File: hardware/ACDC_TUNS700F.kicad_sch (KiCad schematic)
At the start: 1 part, among them U1 TUNS700F28

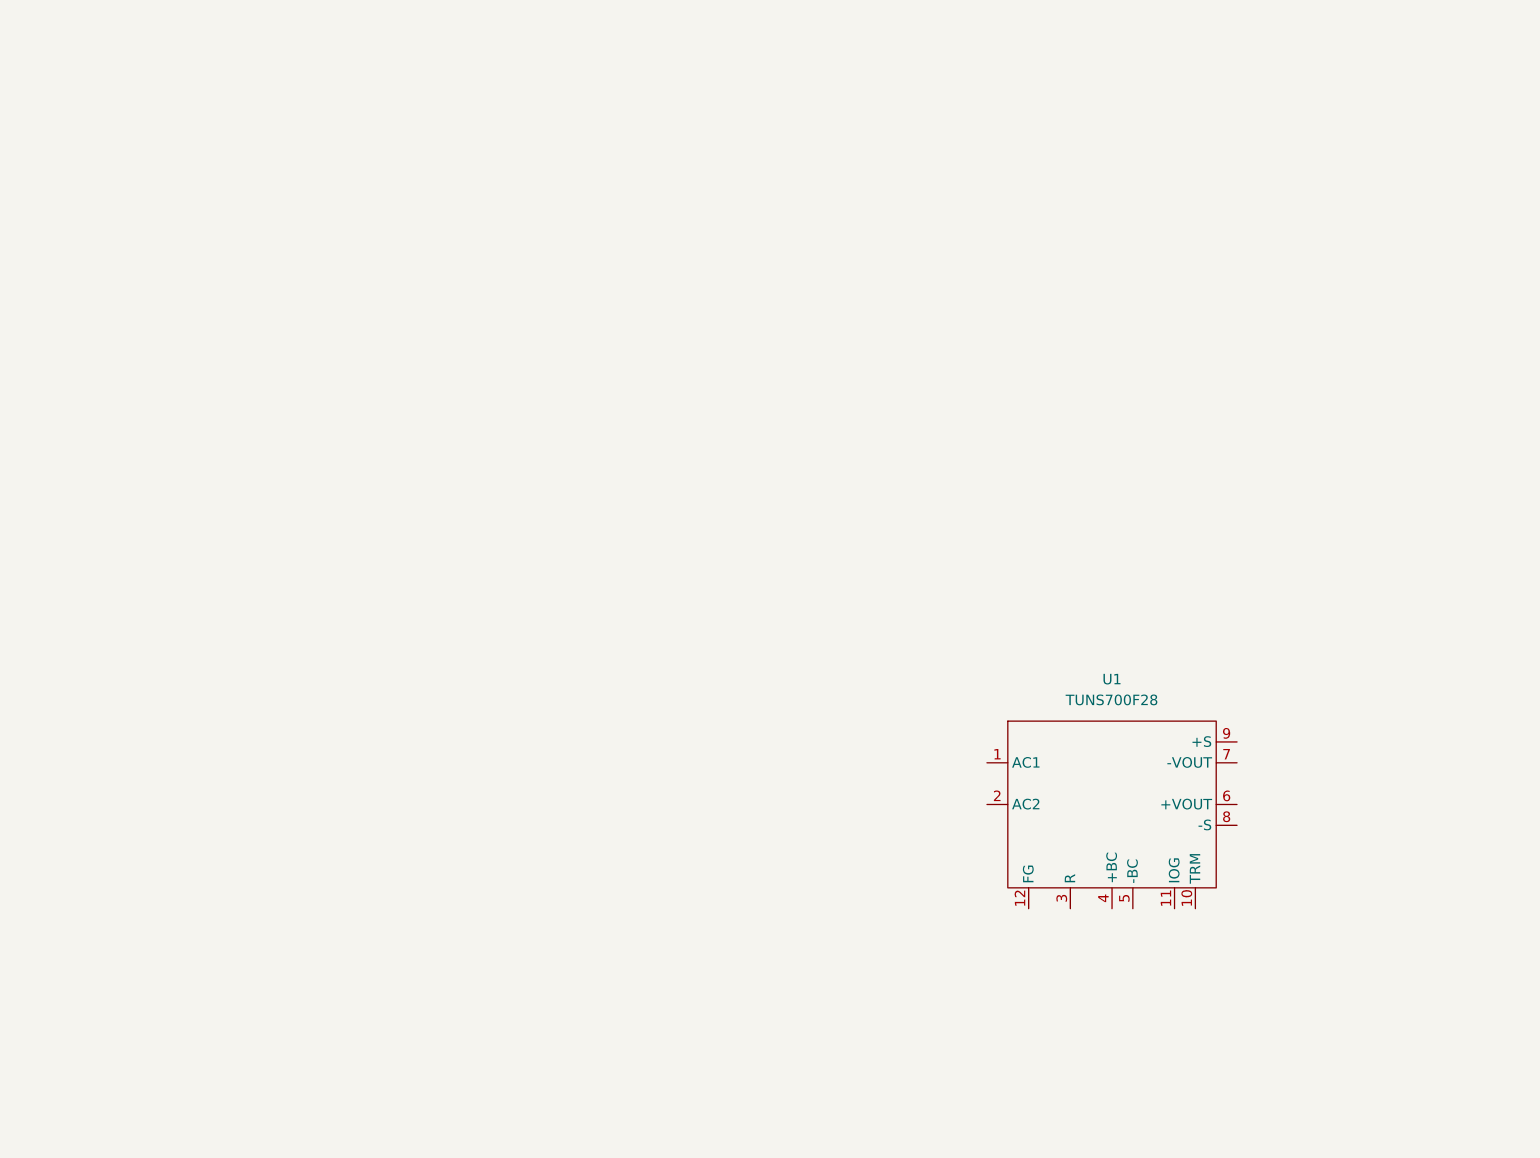
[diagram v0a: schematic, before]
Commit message: input ac filter
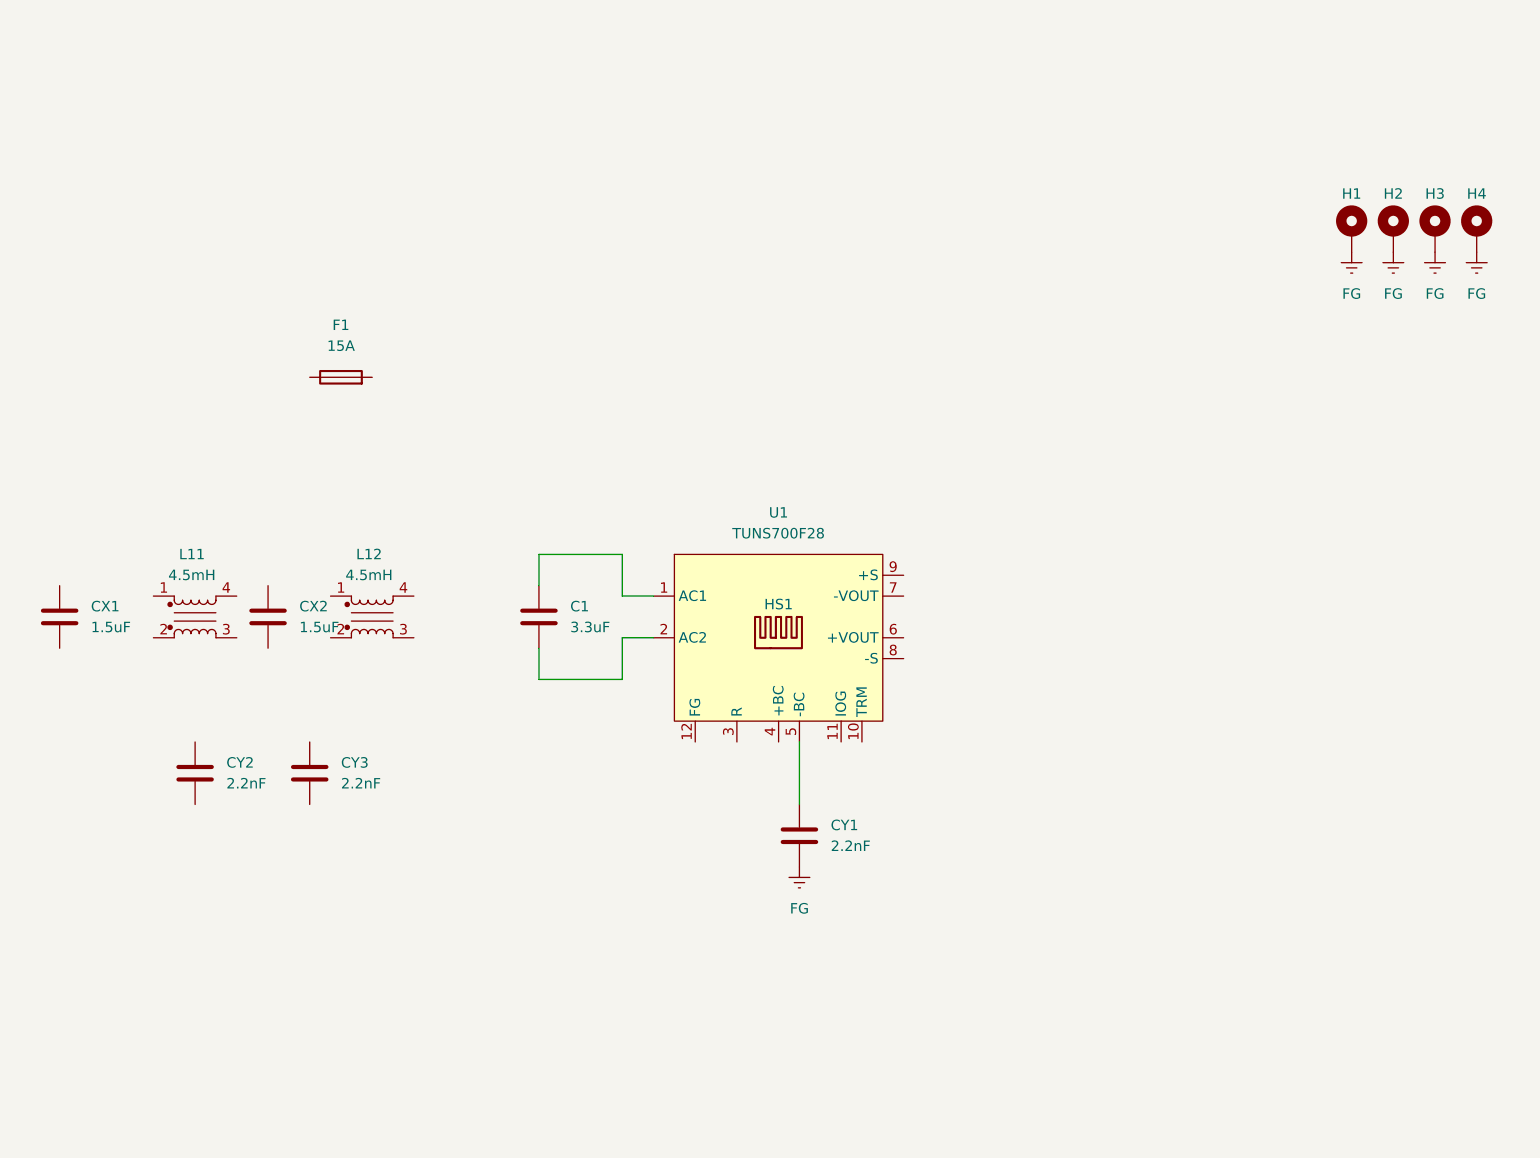
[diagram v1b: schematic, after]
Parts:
- added C1: 3.3uF, ACDC_TUNS700F:CAP-ECQ-UAAF335K, symbol Device:C
- added CX1, CX2: 1.5uF, ACDC_TUNS700F:CAP-ECQ-UAAF155K, symbol Device:C
- added CY1, CY2, CY3: 2.2nF, Capacitor_THT:C_Disc_D9.0mm_W5.0mm_P10.00mm, symbol Device:C
- added F1: 15A, Fuse:Fuseholder_Clip-5x20mm_Littelfuse_100_Inline_P20.50x4.60mm_D1.30mm_Horizontal, symbol Device:Fuse
- added H1, H2, H3, H4: MountingHole_Pad, MountingHole:MountingHole_2.7mm_M2.5_Pad, symbol Mechanical:MountingHole_Pad
- added HS1: ATS1490-ND, symbol Mechanical:Heatsink
- added L11, L12: 4.5mH, ACDC_TUNS700F:CMC_PH9455.405NL, symbol Device:L_Iron_Coupled_1423
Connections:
- net at U1.1 (AC1): now also C1.1
- net at U1.2 (AC2): now also C1.2
- net at U1.5 (-BC): now also CY1.1
- new net FG: CY1.2, H1.1, H2.1, H3.1, H4.1

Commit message: reference schematic complete
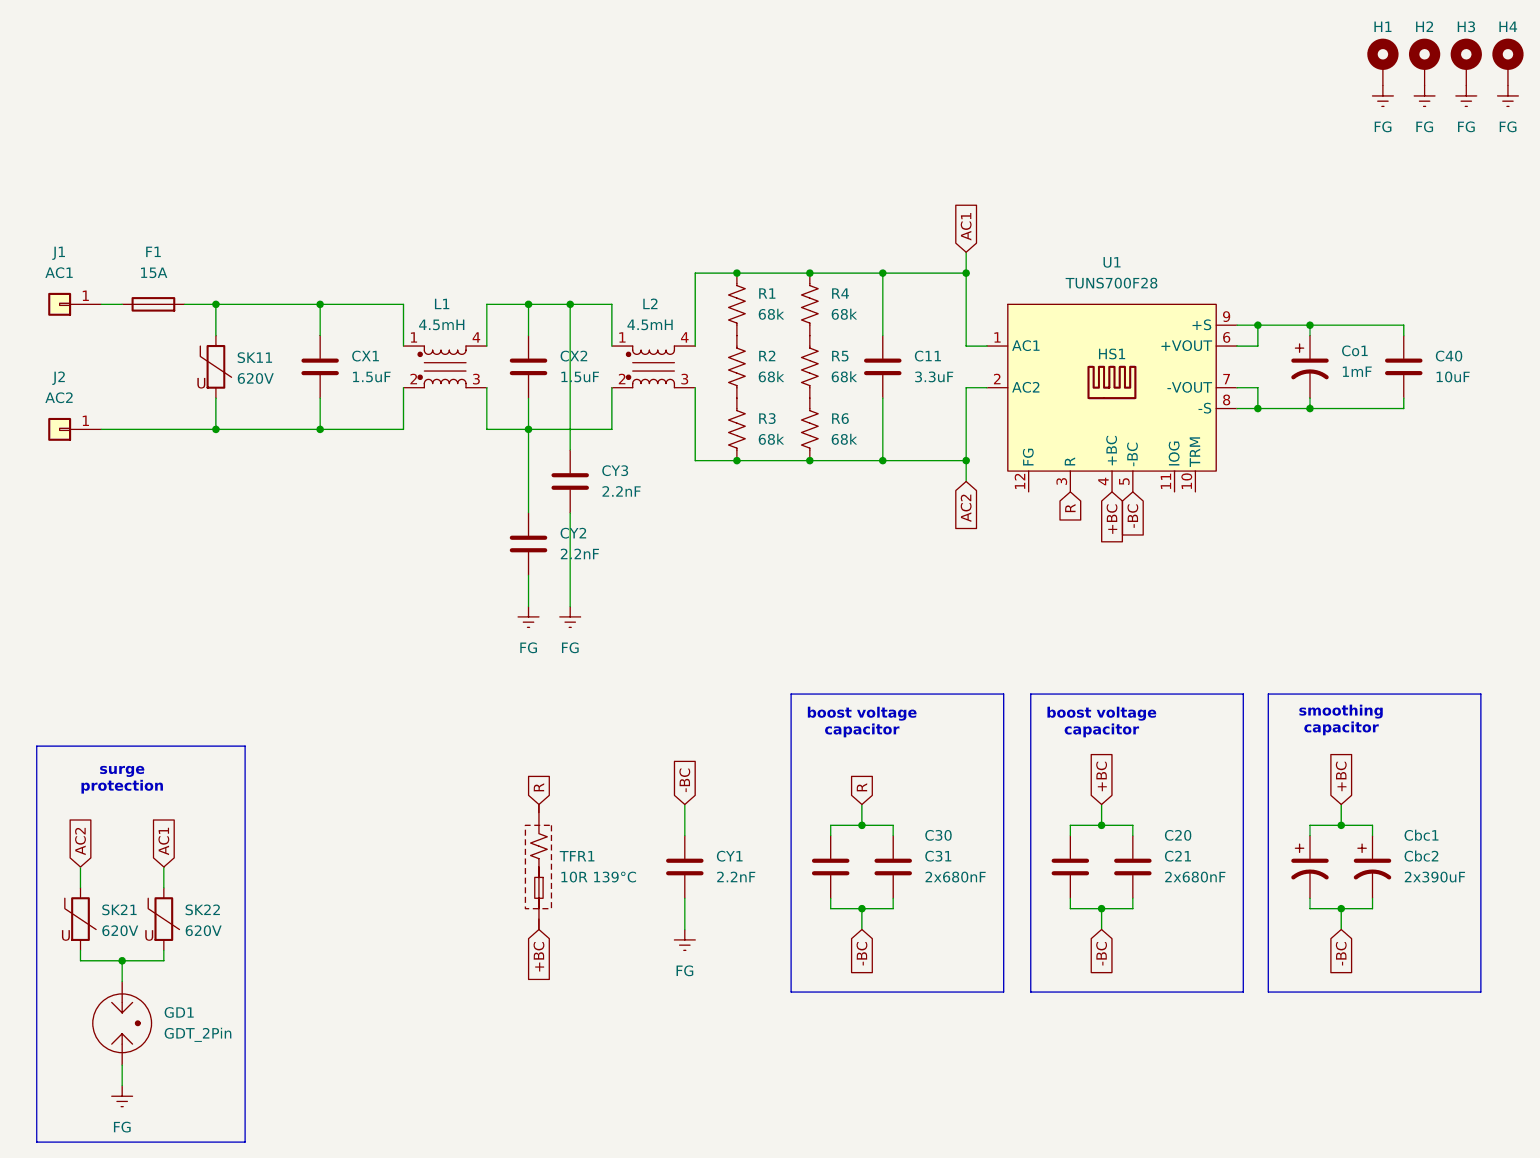
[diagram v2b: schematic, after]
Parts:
- added C20, C30: 680nF, Capacitor_THT:C_Rect_L18.0mm_W8.0mm_P15.00mm_FKS3_FKP3, symbol Device:C
- added C21, C31: 2x680nF, Capacitor_THT:C_Rect_L18.0mm_W8.0mm_P15.00mm_FKS3_FKP3, symbol Device:C
- added C40: 10uF, Capacitor_SMD:C_1206_3216Metric_Pad1.33x1.80mm_HandSolder, symbol Device:C
- added Cbc1, Cbc2: 2x390uF, Capacitor_THT:CP_Radial_D30.0mm_P10.00mm_SnapIn, symbol Device:C_Polarized_US
- added Co1: 1mF, Capacitor_THT:CP_Radial_D16.0mm_P7.50mm, symbol Device:C_Polarized_US
- added GD1: GDT_2Pin, ACDC_TUNS700F:GDT_2093-300-SM-RPLF, symbol Device:GDT_2Pin
- added J1: AC1, symbol Connector_Generic:Conn_01x01
- added J2: AC2, symbol Connector_Generic:Conn_01x01
- added R1, R2, R3, R4, R5, R6: 68k, Resistor_SMD:R_1206_3216Metric_Pad1.30x1.75mm_HandSolder, symbol Device:R_US
- added SK11, SK21, SK22: 620V, ACDC_TUNS700F:RV_Disc_D15,5mm_W7,1mm_P7,5mm, symbol Device:Varistor
- added TFR1: 10R 139°C, ACDC_TUNS700F:TFR_DFP10112, symbol ACDC_TUNS700F:Fuse_Thermal
- renumbered C1 to C11, CY3 to CY2, CY2 to CY3, L11 to L1, L12 to L2
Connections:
- net FG: now also CY2.2, CY3.2, GD1.1
- net AC1: now reaches C11.1, U1.1 (AC1)
- net AC1: now also L2.4, R1.1, R4.1, SK22.1
- net AC2: now reaches C11.2, U1.2 (AC2)
- net AC2: now also L2.3, R3.2, R6.2, SK21.1
- net at CY3.1: now also CX2.1, L1.4, L2.1
- net at L1.1: now also CX1.1, F1.2, SK11.1
- net at L1.2: now also CX1.2, J2.1 (Pin_1), SK11.2
- net at L1.3: now also CX2.2, CY2.1, L2.2
- net at F1.1: now also J1.1 (Pin_1)
- net R: now reaches U1.3 (R)
- net R: now also C30.1, C31.1, TFR1.1
- net +BC: now reaches U1.4 (+BC)
- net +BC: now also C20.1, C21.1, Cbc1.1, Cbc2.1, TFR1.2
- net -BC: now reaches CY1.1, U1.5 (-BC)
- net -BC: now also C20.2, C21.2, C30.2, C31.2, Cbc1.2, Cbc2.2
- net at U1.6 (+VOUT): now also U1.9 (+S), C40.1, Co1.1
- net at U1.7 (-VOUT): now also U1.8 (-S), C40.2, Co1.2
- new net: R4.2, R5.1
- new net: R5.2, R6.1
- new net: GD1.3, SK21.2, SK22.2
- new net: R1.2, R2.1
- new net: R2.2, R3.1
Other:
- note added: "boost voltage capacitor"
- note added: "smoothing capacitor"
- note added: "surge protection"
- moved on the sheet: C11, CX1, CX2, CY1, CY2, CY3, F1, H1, H2, H3, H4, HS1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

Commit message: board layout updates
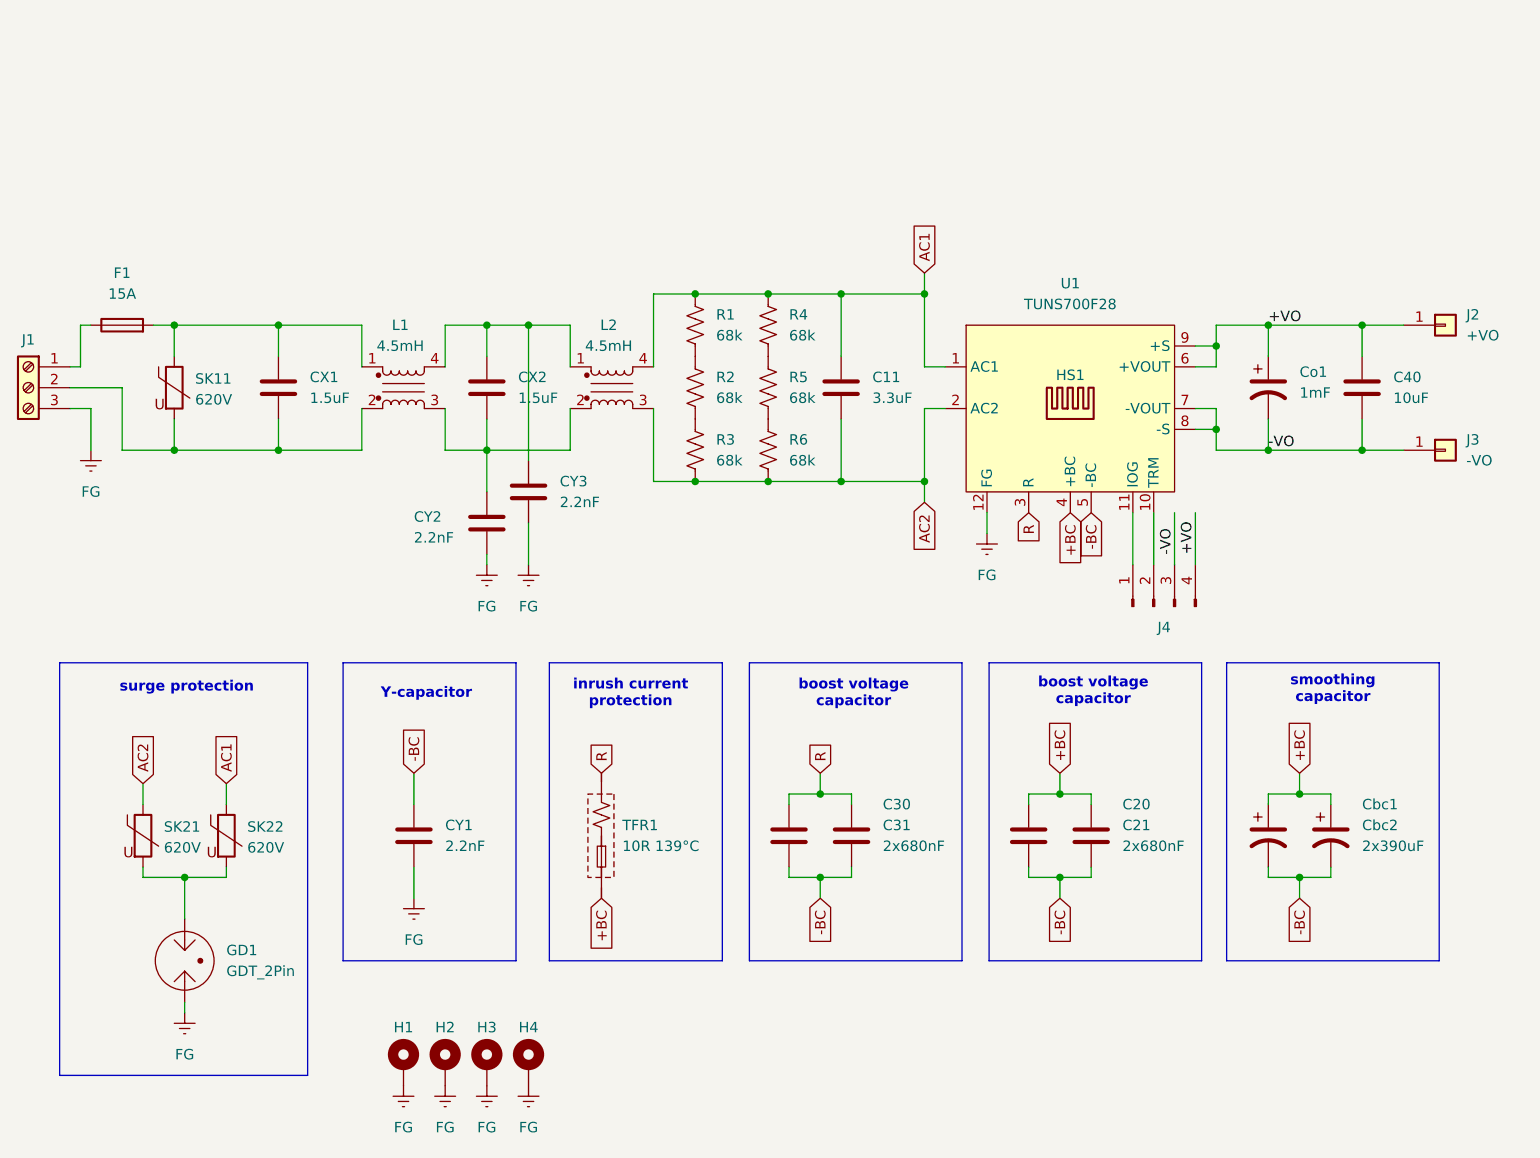
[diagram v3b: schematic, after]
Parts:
- removed J1: AC1, symbol Connector_Generic:Conn_01x01
- added J1: Screw_Terminal_01x03, ACDC_TUNS700F:terminal_NC6-P108-03, symbol Connector:Screw_Terminal_01x03
- added J3: -VO, TerminalBlock_Wuerth:Wuerth_REDCUBE-THR_WP-THRSH_74651194_THR, symbol Connector_Generic:Conn_01x01
- added J4: Conn_01x04_Pin, Connector_PinHeader_2.54mm:PinHeader_1x04_P2.54mm_Vertical, symbol Connector:Conn_01x04_Pin
- J2: value AC2 -> +VO; footprint (none) -> TerminalBlock_Wuerth:Wuerth_REDCUBE-THR_WP-THRSH_74651194_THR; Digi-Key (none) -> 732-74651194RCT-ND
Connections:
- net FG: now also U1.12 (FG), J1.3 (Pin_3)
- net at F1.1: now also J1.1 (Pin_1)
- net +VO: now reaches C40.1, Co1.1, U1.6 (+VOUT), U1.9 (+S)
- net +VO: now also J2.1 (Pin_1), J4.4 (Pin_4)
- net -VO: now reaches C40.2, Co1.2, U1.7 (-VOUT), U1.8 (-S)
- net -VO: now also J3.1 (Pin_1), J4.3 (Pin_3)
- net at CX1.2, L1.2, SK11.2: now also J1.2 (Pin_2); no longer J2.1 (Pin_1)
- net at U1.10 (TRM): now also J4.2 (Pin_2)
- net at U1.11 (IOG): now also J4.1 (Pin_1)
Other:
- note added: "Y-capacitor"
- note added: "inrush current protection"
- company: Flanders Make -> www.reemi.be
- moved on the sheet: C11, C20, C21, C30, C31, C40, CX1, CX2, CY1, CY2, CY3, Cbc1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
